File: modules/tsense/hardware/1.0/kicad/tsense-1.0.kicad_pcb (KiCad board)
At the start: 2 copper layers, 75 x 75 mm, 30 parts, among them J1 Screw_Terminal_01x08, J2 Screw_Terminal_01x08, J3 CAN, SW1 SCR, SW2 INSTANCE, SW3 PRG, U1 Teensy_3.2, U2 MCP2551-I-P, U3 TMR1-1211

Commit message: More code
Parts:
- D1: value SENS -> INST
- D2: value INST -> SRCE
- D3: value SRCE -> SETP
- moved D4 54.1 mm to (152.1, 146.1)
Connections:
- R4 pad 1: /LED_SENSOR -> /LED_INSTANCE
- R5 pad 1: /LED_INSTANCE -> /LED_SOURCE
- R6 pad 1: /LED_SOURCE -> /LED_SETPOINT
- U1 pad 2: /LED_SOURCE -> /LED_SETPOINT
- U1 pad 3: /LED_INSTANCE -> /LED_SOURCE
- U1 pad 4: /LED_SENSOR -> /LED_INSTANCE
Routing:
- net Net-(D4-Pad2): track 60.0 -> 6.35 mm
- net /LED_SETPOINT: track 0.00 -> 5.72 mm
- net /LED_SENSOR: track 5.72 -> 0.00 mm
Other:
- board text added: "NMEA 2000 Temperature Sensor Module"
- board text added: "PWR/TX"
- board text added: "TSENSE"
- board text removed: "DOWN"
- board text removed: "NMEA 2000 Windlass Interface Module"
- board text removed: "PWR/RX"
- board text removed: "UP"
- board text removed: "WINT"

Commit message: More code
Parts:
- removed RN1: 2.2K, Resistor_THT:R_Array_SIP9
- added R2: 2K2, Resistor_THT:R_Axial_DIN0204_L3.6mm_D1.6mm_P5.08mm_Horizontal, F.Cu at (166.0, 125.7)
- added R3: 2K2, Resistor_THT:R_Axial_DIN0204_L3.6mm_D1.6mm_P5.08mm_Horizontal, F.Cu at (166.0, 128.3)
- added R4: 2K2, Resistor_THT:R_Axial_DIN0204_L3.6mm_D1.6mm_P5.08mm_Horizontal, F.Cu at (166.0, 130.8)
- added R5: 2K2, Resistor_THT:R_Axial_DIN0204_L3.6mm_D1.6mm_P5.08mm_Horizontal, F.Cu at (166.0, 133.3)
- added R6: 2K2, Resistor_THT:R_Axial_DIN0204_L3.6mm_D1.6mm_P5.08mm_Horizontal, F.Cu at (166.0, 143.5)
- added R7: 2K2, Resistor_THT:R_Axial_DIN0204_L3.6mm_D1.6mm_P5.08mm_Horizontal, F.Cu at (166.0, 141.0)
- added R8: 2K2, Resistor_THT:R_Axial_DIN0204_L3.6mm_D1.6mm_P5.08mm_Horizontal, F.Cu at (166.0, 138.4)
- added R9: 2K2, Resistor_THT:R_Axial_DIN0204_L3.6mm_D1.6mm_P5.08mm_Horizontal, F.Cu at (166.0, 135.9)
- J1, J2: footprint PDJR:WAGO-250-108 -> PDJR-connectors:Phoenix-FK-MPT-8-3,5
- SW1: renamed from SW3; footprint Button_Switch_THT:KSA_Tactile_SPST -> Button_Switch_THT:SW_PUSH_6mm_H4.3mm
- moved J1 5.10 mm to (202.0, 128.5)
- moved J2 5.10 mm to (145.0, 128.5), turned to 90 degrees
- moved SW1 4.58 mm to (195.0, 110.0), turned to 90 degrees
- renumbered R4 to R1, R5 to R10, R6 to R11, R7 to R12, R2 to R13, R3 to R14, R1 to R15, SW1 to SW2, SW2 to SW3, U3 to U2, U2 to U3
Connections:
- J2 pad 1: /SENSOR_T4 -> /SENSOR_T7
- J2 pad 3: /SENSOR_T5 -> /SENSOR_T6
- J2 pad 5: /SENSOR_T6 -> /SENSOR_T5
- J2 pad 7: /SENSOR_T7 -> /SENSOR_T4
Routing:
- net /SENSOR_T3: track 79.0 -> 64.7 mm
- net /SENSOR_T2: track 72.7 -> 61.5 mm
- net Net-(SW1-Pad2): track 156.0 -> 147.9 mm
- net /SENSOR_T1: track 68.1 -> 60.0 mm
- net +5V: track 164.6 -> 156.9 mm
- net /SENSOR_T0: track 61.3 -> 55.2 mm
- net /CAN_SCR: track 20.7 -> 18.4 mm
- net /SENSOR_T6: track 28.8 -> 26.6 mm
- net /SENSOR_T4: track 36.2 -> 37.3 mm

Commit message: PCB tweaks
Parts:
- added TEST: PinHeader_1x02_P2.54mm_Vertical, Connector_PinHeader_2.54mm:PinHeader_1x02_P2.54mm_Vertical, F.Cu at (138.9, 105.4)
- C1, C2, C3, C4: footprint Capacitor_THT:CP_Radial_D5.0mm_P2.50mm -> Capacitor_THT:C_Rect_L4.6mm_W3.0mm_P2.50mm_MKS02_FKP02
- SW3: value INSTANCE -> PRG-VALUE
- moved C1 3.80 mm to (163.8, 156.2)
- moved R12 2.54 mm to (166.0, 148.6)
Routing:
- net Net-(SW1-Pad2): track 147.9 -> 120.5 mm
- net /SENSOR_T0: track 55.2 -> 72.8 mm
- net +5V: track 156.9 -> 170.9 mm
- net /SENSOR_T1: track 60.0 -> 71.8 mm
- net GND: track 0.00 -> 9.65 mm
- net /SENSOR_T2: track 61.5 -> 70.0 mm
- net Net-(D2-Pad2): track 61.4 -> 69.6 mm
- net Net-(D3-Pad2): track 66.1 -> 73.4 mm
- net /SENSOR_T4: track 37.3 -> 30.4 mm
- net /SENSOR_T3: track 64.7 -> 68.8 mm
- net /SENSOR_T5: track 32.1 -> 28.4 mm
- net Net-(D4-Pad2): track 6.35 -> 8.89 mm
- net /LED_PWR: track 5.08 -> 2.54 mm
- net /CAN_L: track 17.0 -> 18.8 mm
- net Net-(D1-Pad2): track 51.0 -> 50.0 mm
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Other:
- board text added: "GND"
- board text added: "TO PROGRAM 1. Select sensor using PRG-VALUE. Press PRG. 2. Set binary instance using PRG-VALUE. Press PRG. 3. Set binary source using PRG-VALUE. Press PRG. 4. Set binary set temp using PRG-VALUE. Press PRG."
- board text added: "Vcc"

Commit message: Some code
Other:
- board text added: "VCC"
- board text removed: "Vcc"

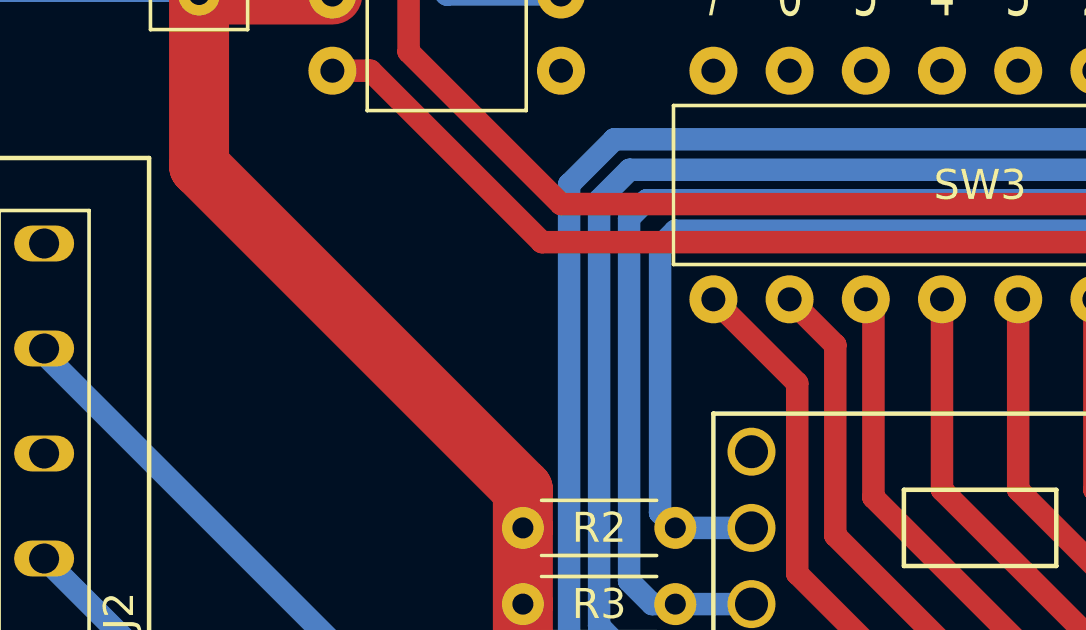
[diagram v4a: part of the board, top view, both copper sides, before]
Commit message: Add text to PCB
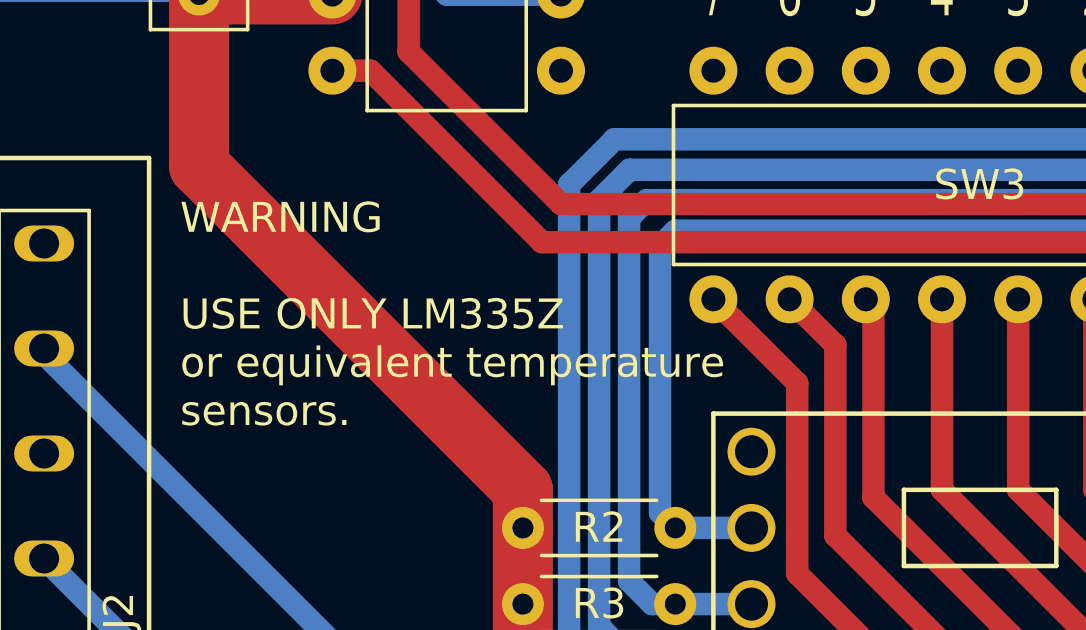
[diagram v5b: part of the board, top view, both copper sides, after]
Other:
- board text added: "WARNING USE ONLY LM335Z or equivalent temperature sensors."
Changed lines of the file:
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@@
-(kicad_pcb (version 20171130) (host pcbnew 5.1.9-73d0e3b20d~88~ubuntu20.04.1)
+(kicad_pcb (version 20171130) (host pcbnew 5.1.5-1.fc31)
   (general
     (thickness 1.6)
-    (drawings 133)
+    (drawings 134)
     (tracks 219)
     (zones 0)
@@
     )
   )
+  (gr_text "WARNING\n\nUSE ONLY LM335Z\nor equivalent temperature\nsensors." (at 149.53 118.618) (layer F.SilkS)
+    (effects (font (size 1 1) (thickness 0.15)) (justify left))
+  )
   (gr_text VCC (at 142.164 107.95) (layer F.SilkS)

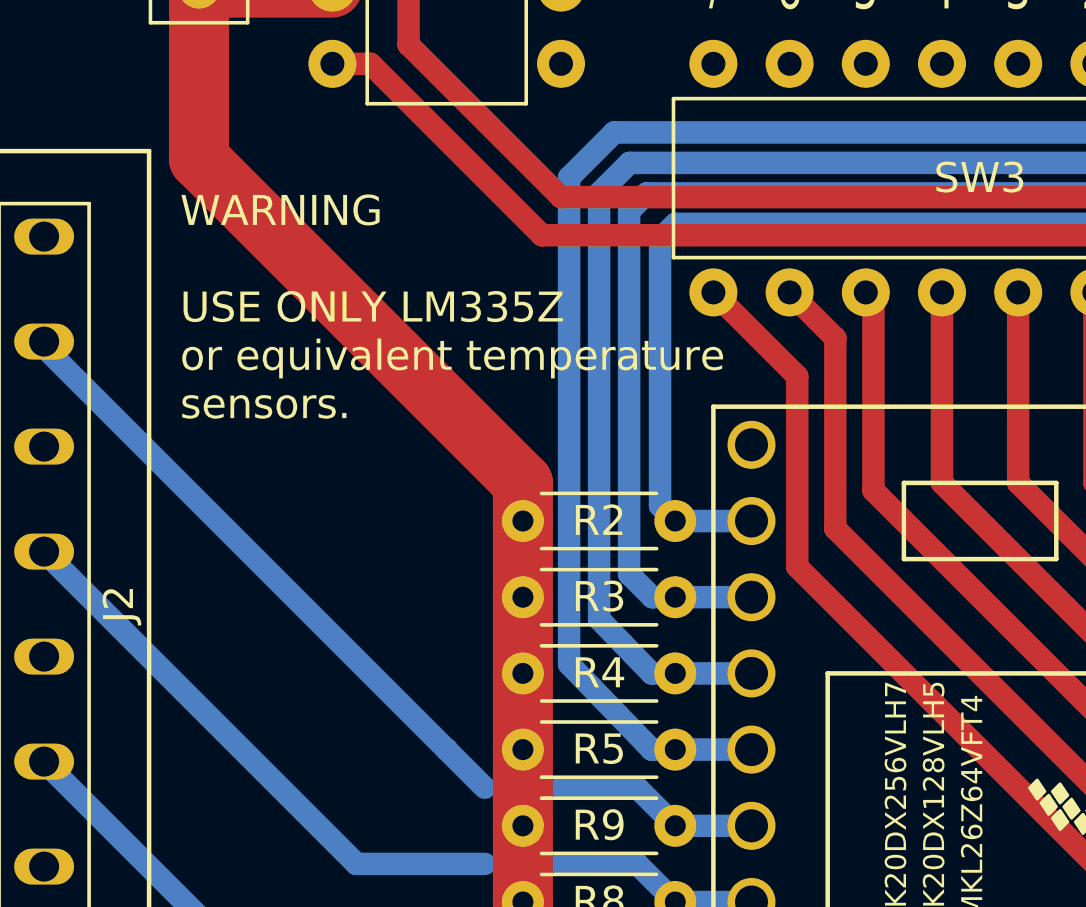
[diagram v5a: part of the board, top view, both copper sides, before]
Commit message: Correct temperature computation
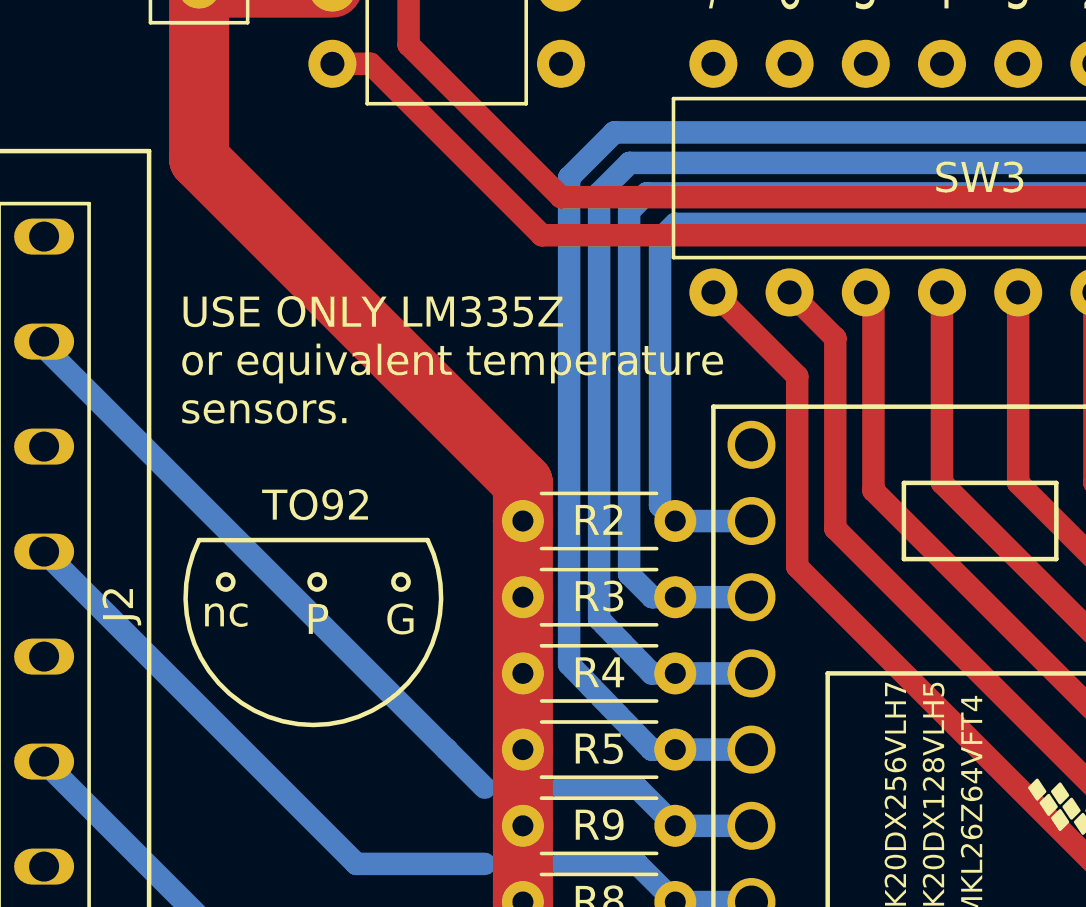
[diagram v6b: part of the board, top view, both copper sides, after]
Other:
- board text added: "TO92"
- board text added: "USE ONLY LM335Z or equivalent temperature sensors."
- board text added: "nc"
- board text removed: "WARNING USE ONLY LM335Z or equivalent temperature sensors."
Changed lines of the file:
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@@
-(kicad_pcb (version 20171130) (host pcbnew 5.1.5-1.fc31)
+(kicad_pcb (version 20171130) (host pcbnew 5.1.9-73d0e3b20d~88~ubuntu20.04.1)
   (general
     (thickness 1.6)
-    (drawings 134)
+    (drawings 143)
     (tracks 219)
     (zones 0)
@@
     (33 F.Adhes user hide)
     (35 F.Paste user hide)
-    (37 F.SilkS user)
+    (37 F.SilkS user hide)
     (38 B.Mask user hide)
     (39 F.Mask user hide)
     (40 Dwgs.User user hide)
     (41 Cmts.User user hide)
-    (42 Eco1.User user)
+    (42 Eco1.User user hide)
     (43 Eco2.User user hide)
     (44 Edge.Cuts user)
@@
     )
   )
-  (gr_text "WARNING\n\nUSE ONLY LM335Z\nor equivalent temperature\nsensors." (at 149.53 118.618) (layer F.SilkS)
+  (gr_text TO92 (at 154.102 125.222) (layer F.SilkS)
+    (effects (font (size 1 1) (thickness 0.15)))
+  )
+  (gr_text nc (at 151.054 128.778) (layer F.SilkS)
+    (effects (font (size 1 1) (thickness 0.15)))
+  )
+  (gr_text P (at 154.102 129.032) (layer F.SilkS)
+    (effects (font (size 1 1) (thickness 0.15)))
+  )
+  (gr_text G (at 156.896 129.032) (layer F.SilkS)
+    (effects (font (size 1 1) (thickness 0.15)))
+  )
+  (gr_circle (center 156.896 127.762) (end 156.642 127.762) (layer F.SilkS) (width 0.15))
+  (gr_circle (center 151.054 127.762) (end 151.308 127.762) (layer F.SilkS) (width 0.15))
+  (gr_circle (center 154.102 127.762) (end 154.356 127.762) (layer F.SilkS) (width 0.15))
+  (gr_arc (start 153.975 128.27) (end 150.165001 126.365001) (angle -233.1301024) (layer F.SilkS) (width 0.15))
+  (gr_line (start 150.165 126.365) (end 157.785 126.365) (layer F.SilkS) (width 0.15))
+  (gr_text "USE ONLY LM335Z\nor equivalent temperature\nsensors." (at 149.53 120.396) (layer F.SilkS)
     (effects (font (size 1 1) (thickness 0.15)) (justify left))
   )

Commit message: Create Gerber files
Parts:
- U2: value TMR1-1211 -> TMR-1-1211; footprint Converter_DCDC:Converter_DCDC_TRACO_TMR-xxxx_THT -> PDJR-connectors:TMR-1-1211
- moved U2 5.44 mm to (188.4, 93.2)
- moved SW2 1.02 mm to (138.9, 97.5)
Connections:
- net /NET_S renamed Net-(F1-Pad1)
- U2 pad 6: +5V -> GND
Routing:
- net Net-(F1-Pad2): track 26.2 -> 19.6 mm
- net /NET_C: track 39.0 -> 42.2 mm
- net +5V: track 170.9 -> 168.0 mm
- net Net-(F1-Pad1): track 48.4 -> 49.1 mm
